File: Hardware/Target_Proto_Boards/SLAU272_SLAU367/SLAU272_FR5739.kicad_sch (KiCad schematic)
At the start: 38 parts, among them J1 USB_B_Micro, J10 GND, J11 +5V, J12 GND, J13 VSEL, J2 DEBUG, J3 PORT1, J4 LED_P4.1, J5 PORT2, J6 LogicAna, J7 JTAG/SBW, J8 PORT3, J9 VCC, SW1 TL-2203, SW2 RESET, U1 AMS1117-3.3, U2 MSP430FR5739IDAR, Y1 16M

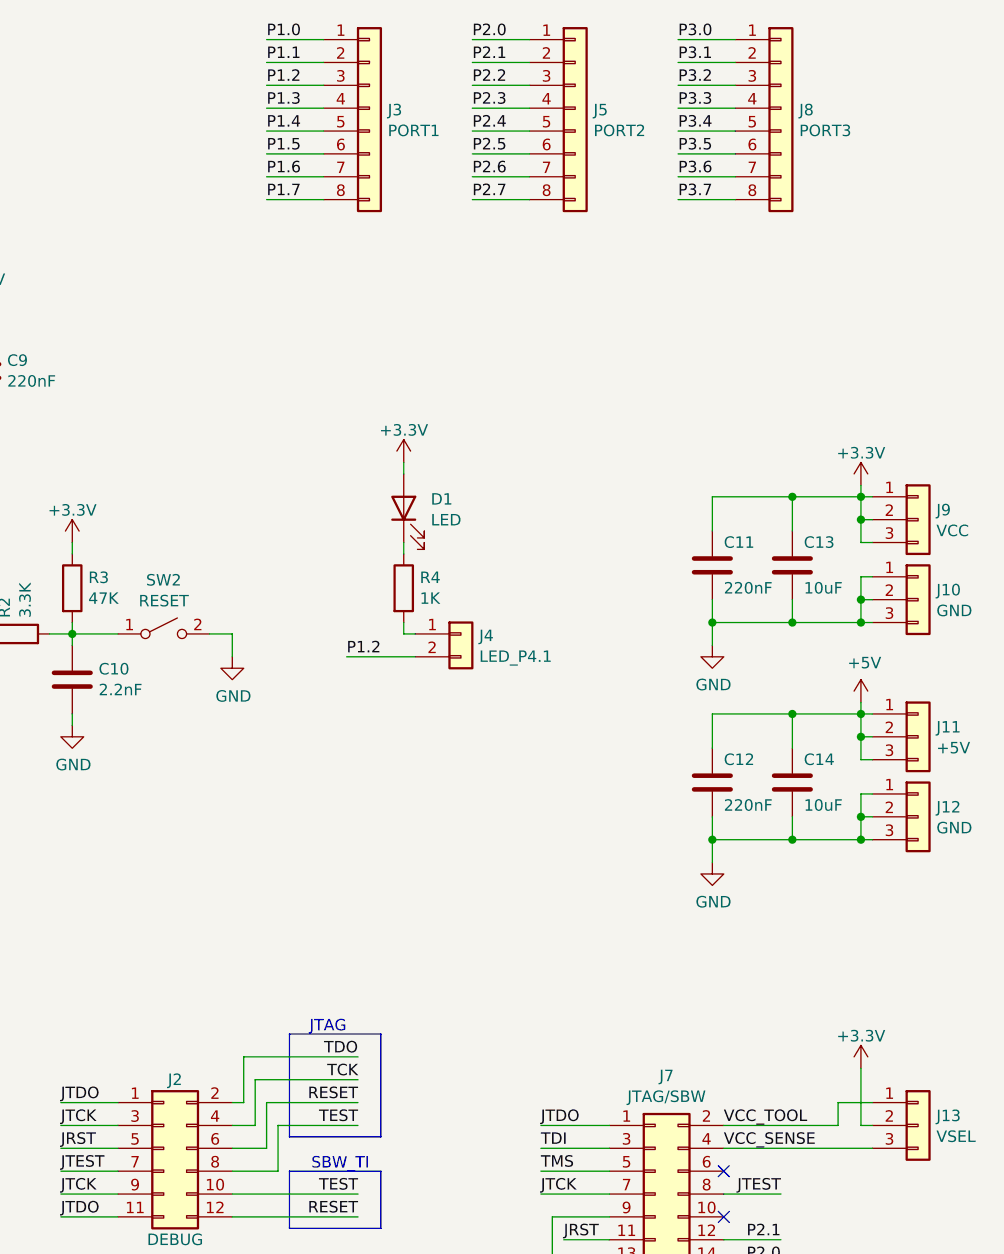
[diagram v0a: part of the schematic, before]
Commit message: Changed SLAU272_SLAU367 proto board to fully support FR5858 chips
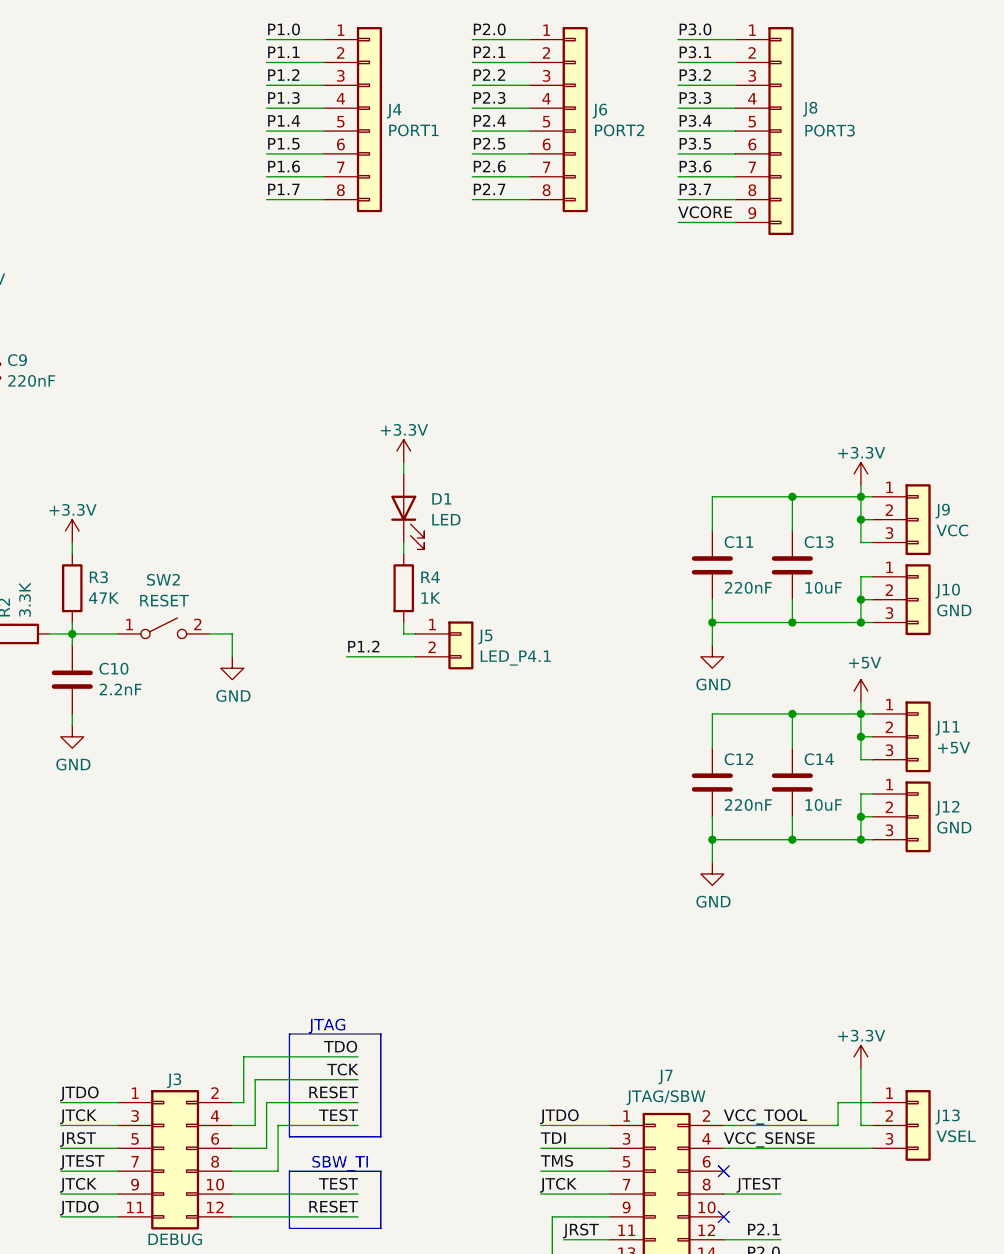
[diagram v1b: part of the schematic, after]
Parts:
- C8: Descr X5R ±10% 50V 1uF 0603 Multilayer Ceramic Capacitors MLCC - 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 -> (none); LCSC C15849 -> (none)
- J8: footprint Connector_PinHeader_2.54mm:PinHeader_1x08_P2.54mm_Vertical -> Connector_PinHeader_2.54mm:PinHeader_1x09_P2.54mm_Vertical; symbol Connector_Generic:Conn_01x08 -> Connector_Generic:Conn_01x09
- renumbered J6 to J2, J2 to J3, J3 to J4, J4 to J5, J5 to J6
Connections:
- net VCORE: now also J8.9 (Pin_9)

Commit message: Documentation for SLAU272_SLAU367 proto-board
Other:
- title: MSP430 FR2476 Proto board -> MSP430 FR5739 Proto board
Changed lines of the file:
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@@
   (paper "A4")
   (title_block
-    (title "MSP430 FR2476 Proto board")
-    (date "2022-09-11")
-    (rev "1.2")
+    (title "MSP430 FR5739 Proto board")
+    (date "2022-09-14")
+    (rev "1.0")
     (company "Mathias Gruber")
   )

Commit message: Added proto-board production files.
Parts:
- Y1: footprint Crystal:Resonator_SMD_Murata_CSTxExxV-3Pin_3.0x1.1mm_HandSoldering -> Crystal:Resonator_SMD_Murata_CSTxExxV-3Pin_3.0x1.1mm
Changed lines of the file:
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@@
       (effects (font (size 1.27 1.27)) (justify left))
     )
-    (property "Footprint" "Crystal:Resonator_SMD_Murata_CSTxExxV-3Pin_3.0x1.1mm_HandSoldering" (id 2) (at 101.6 132.715 0)
+    (property "Footprint" "Crystal:Resonator_SMD_Murata_CSTxExxV-3Pin_3.0x1.1mm" (id 2) (at 101.6 132.715 0)
       (effects (font (size 1.27 1.27)) hide)
     )
@@
     )
     (path "/00000000-0000-0000-0000-00006144b8ff"
-      (reference "Y1") (unit 1) (value "16M") (footprint "Crystal:Resonator_SMD_Murata_CSTxExxV-3Pin_3.0x1.1mm_HandSoldering")
-    )
-  )
+      (reference "Y1") (unit 1) (value "16M") (footprint "Crystal:Resonator_SMD_Murata_CSTxExxV-3Pin_3.0x1.1mm")
+    )
+  )

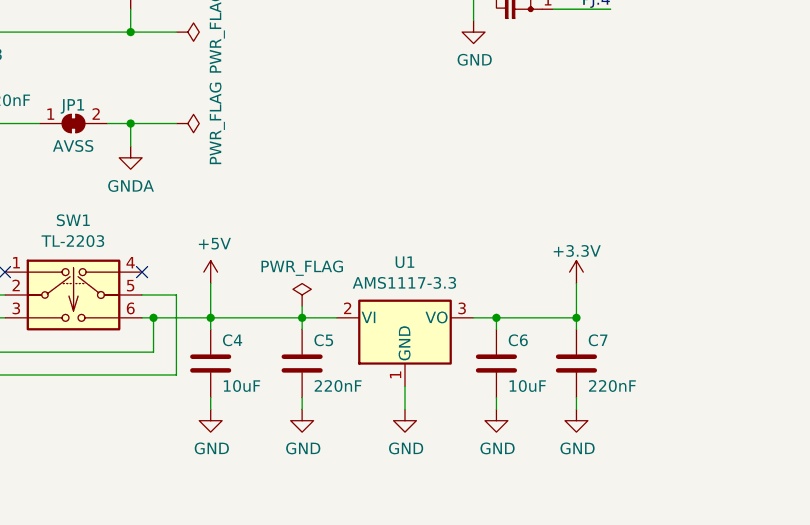
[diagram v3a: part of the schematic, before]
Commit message: Fixed regulator part#
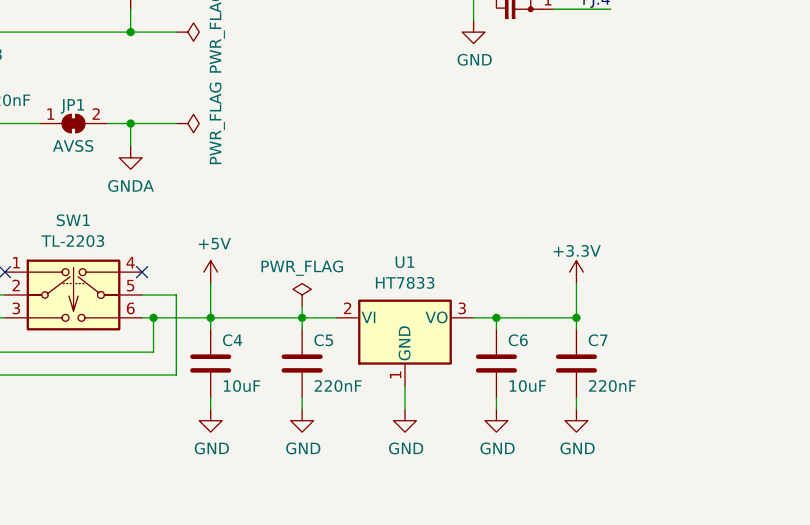
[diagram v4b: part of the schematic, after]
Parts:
- U1: value AMS1117-3.3 -> HT7833
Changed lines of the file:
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@@
     (in_bom yes) (on_board yes)
     (property "Reference" "U1" (id 0) (at 87.63 162.7632 0))
-    (property "Value" "AMS1117-3.3" (id 1) (at 87.63 165.0746 0))
+    (property "Value" "HT7833" (id 1) (at 87.63 165.0746 0))
     (property "Footprint" "Package_TO_SOT_SMD:SOT-89-3_Handsoldering" (id 2) (at 87.63 163.83 0)
       (effects (font (size 1.27 1.27)) hide)
@@
     )
     (path "/00000000-0000-0000-0000-0000610e48b7"
-      (reference "U1") (unit 1) (value "AMS1117-3.3") (footprint "Package_TO_SOT_SMD:SOT-89-3_Handsoldering")
+      (reference "U1") (unit 1) (value "HT7833") (footprint "Package_TO_SOT_SMD:SOT-89-3_Handsoldering")
     )
     (path "/00000000-0000-0000-0000-00006119fd0e"
